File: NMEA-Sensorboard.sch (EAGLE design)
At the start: 15 parts, among them IC1 R-78E05-1.0, IC2 ESP32_D1_MINI, IC3 MCP2562, IC4 INA226, X3 DS1820, X4 DS1820, X5 DS1820, X6 DS1820, X7 BUS

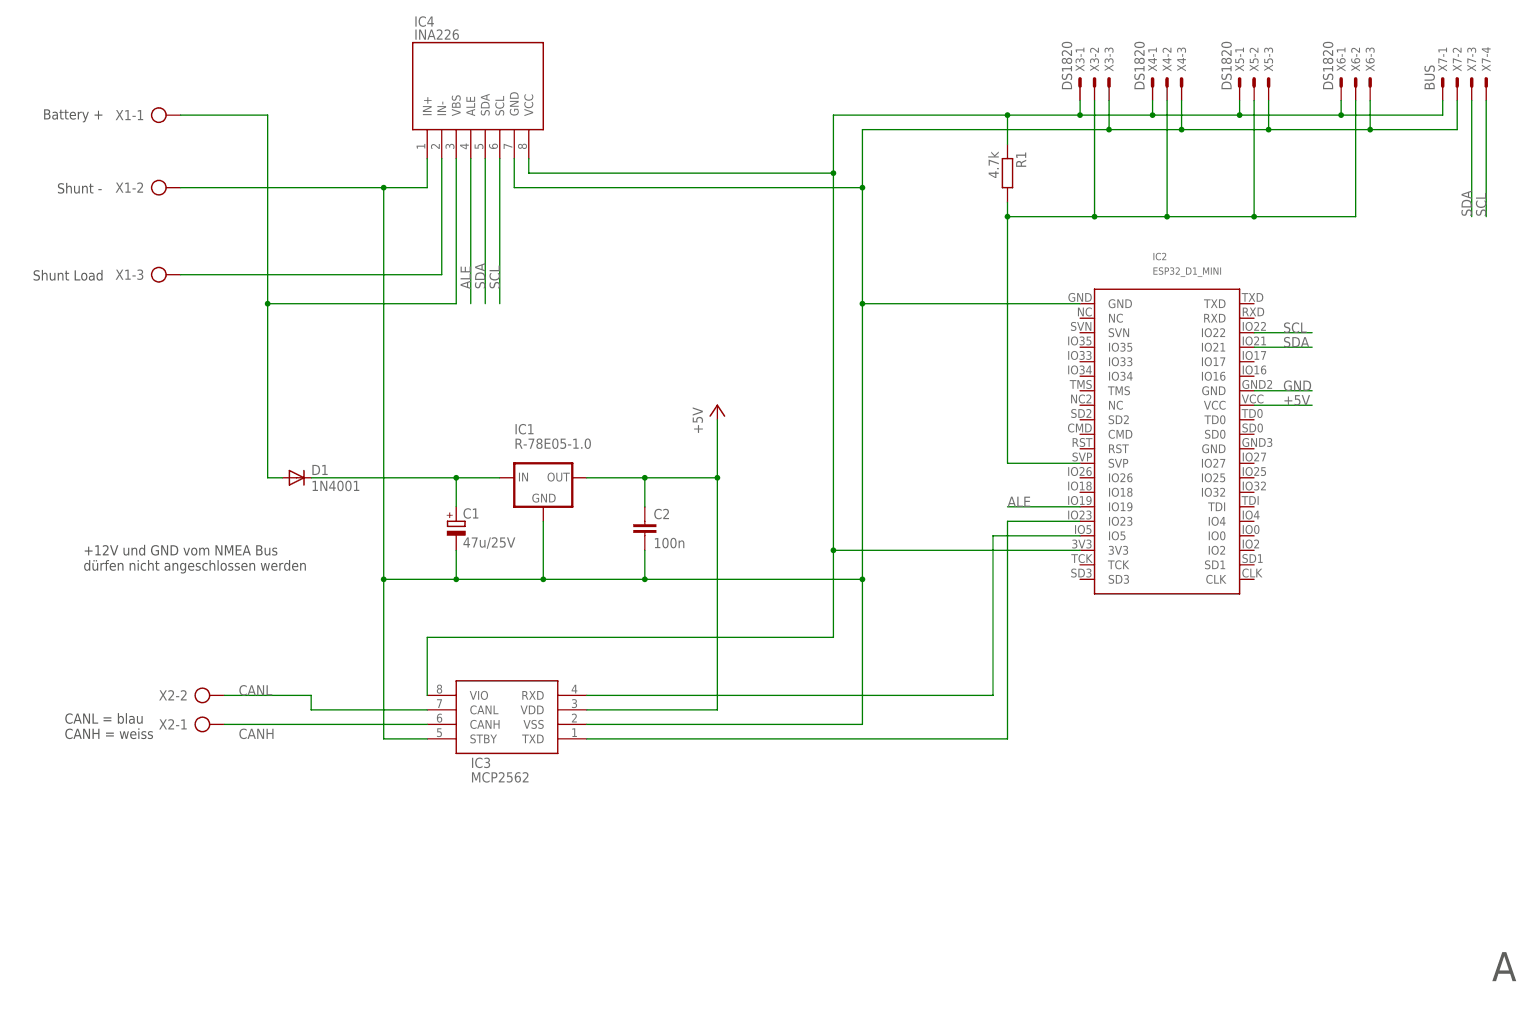
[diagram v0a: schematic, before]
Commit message: refactor: overhaul schematic and PCB layout to fix multiple issues
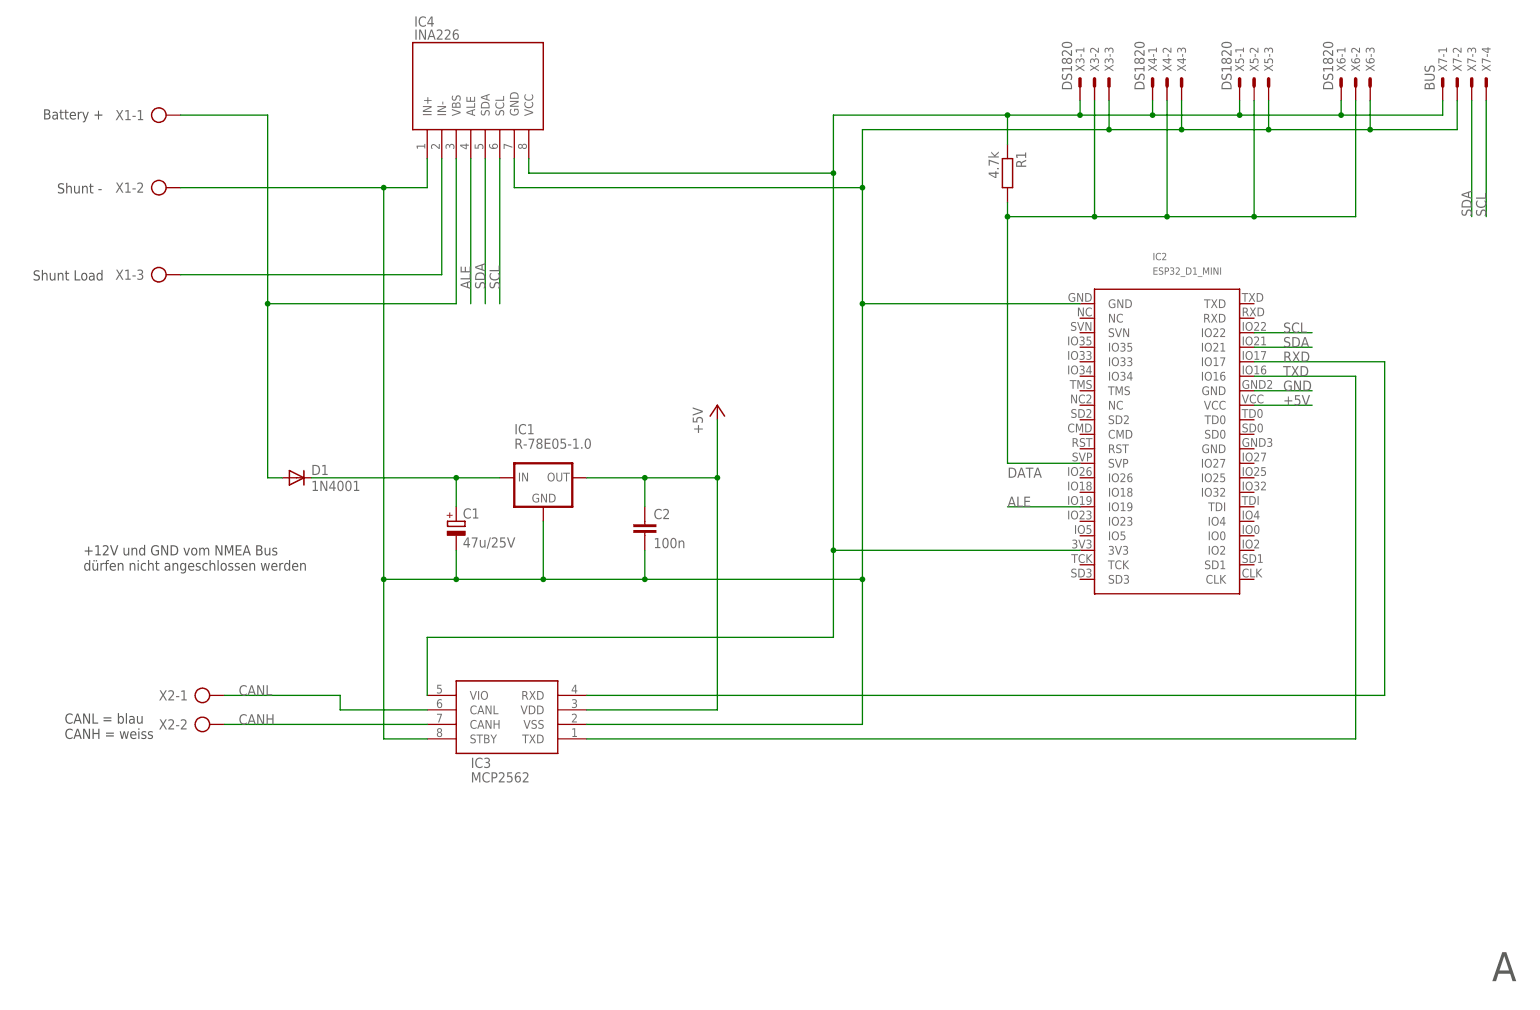
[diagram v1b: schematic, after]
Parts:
- C1: device rcl:CPOL-EUE5-8.5 -> rcl:CPOL-EUE2-5
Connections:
- net N$9 renamed DATA
- net CANH: now also X2-2.KL; no longer X2-1.KL
- net CANL: now also X2-1.KL; no longer X2-2.KL
- net RXD: now also IC2.IO17; no longer IC2.IO5
- net TXD: now also IC2.IO16; no longer IC2.IO23
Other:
- moved on the sheet: X2-1, X2-2
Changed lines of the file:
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@@
 <grid distance="0.1" unitdist="inch" unit="inch" style="lines" multiple="1" display="no" altdistance="0.01" altunitdist="inch" altunit="inch"/>
 <layers>
-<layer number="1" name="Top" color="4" fill="1" visible="no" active="no"/>
-<layer number="16" name="Bottom" color="1" fill="1" visible="no" active="no"/>
-<layer number="17" name="Pads" color="2" fill="1" visible="no" active="no"/>
-<layer number="18" name="Vias" color="2" fill="1" visible="no" active="no"/>
-<layer number="19" name="Unrouted" color="6" fill="1" visible="no" active="no"/>
-<layer number="20" name="Dimension" color="24" fill="1" visible="no" active="no"/>
-<layer number="21" name="tPlace" color="7" fill="1" visible="no" active="no"/>
-<layer number="22" name="bPlace" color="7" fill="1" visible="no" active="no"/>
-<layer number="23" name="tOrigins" color="15" fill="1" visible="no" active="no"/>
-<layer number="24" name="bOrigins" color="15" fill="1" visible="no" active="no"/>
-<layer number="25" name="tNames" color="7" fill="1" visible="no" active="no"/>
-<layer number="26" name="bNames" color="7" fill="1" visible="no" active="no"/>
-<layer number="27" name="tValues" color="7" fill="1" visible="no" active="no"/>
-<layer number="28" name="bValues" color="7" fill="1" visible="no" active="no"/>
+<layer number="1" name="Top" color="4" fill="1" visible="yes" active="no"/>
+<layer number="16" name="Bottom" color="1" fill="1" visible="yes" active="no"/>
+<layer number="17" name="Pads" color="2" fill="1" visible="yes" active="no"/>
+<layer number="18" name="Vias" color="2" fill="1" visible="yes" active="no"/>
+<layer number="19" name="Unrouted" color="6" fill="1" visible="yes" active="no"/>
+<layer number="20" name="Dimension" color="24" fill="1" visible="yes" active="no"/>
+<layer number="21" name="tPlace" color="7" fill="1" visible="yes" active="no"/>
+<layer number="22" name="bPlace" color="7" fill="1" visible="yes" active="no"/>
+<layer number="23" name="tOrigins" color="15" fill="1" visible="yes" active="no"/>
+<layer number="24" name="bOrigins" color="15" fill="1" visible="yes" active="no"/>
+<layer number="25" name="tNames" color="7" fill="1" visible="yes" active="no"/>
+<layer number="26" name="bNames" color="7" fill="1" visible="yes" active="no"/>
+<layer number="27" name="tValues" color="7" fill="1" visible="yes" active="no"/>
+<layer number="28" name="bValues" color="7" fill="1" visible="yes" active="no"/>
 <layer number="29" name="tStop" color="7" fill="3" visible="no" active="no"/>
 <layer number="30" name="bStop" color="7" fill="6" visible="no" active="no"/>
@@
 <layer number="35" name="tGlue" color="7" fill="4" visible="no" active="no"/>
 <layer number="36" name="bGlue" color="7" fill="5" visible="no" active="no"/>
-<layer number="37" name="tTest" color="7" fill="1" visible="no" active="no"/>
-<layer number="38" name="bTest" color="7" fill="1" visible="no" active="no"/>
+<layer number="37" name="tTest" color="7" fill="1" visible="yes" active="no"/>
+<layer number="38" name="bTest" color="7" fill="1" visible="yes" active="no"/>
 <layer number="39" name="tKeepout" color="4" fill="11" visible="no" active="no"/>
 <layer number="40" name="bKeepout" color="1" fill="11" visible="no" active="no"/>
@@
 <layer number="44" name="Drills" color="7" fill="1" visible="no" active="no"/>
 <layer number="45" name="Holes" color="7" fill="1" visible="no" active="no"/>
-<layer number="46" name="Milling" color="3" fill="1" visible="no" active="no"/>
-<layer number="47" name="Measures" color="7" fill="1" visible="no" active="no"/>
-<layer number="48" name="Document" color="7" fill="1" visible="no" active="no"/>
-<layer number="49" name="Reference" color="7" fill="1" visible="no" active="no"/>
-<layer number="51" name="tDocu" color="7" fill="1" visible="no" active="no"/>
-<layer number="52" name="bDocu" color="7" fill="1" visible="no" active="no"/>
+<layer number="46" name="Milling" color="3" fill="1" visible="yes" active="no"/>
+<layer number="47" name="Measures" color="7" fill="1" visible="yes" active="no"/>
+<layer number="48" name="Document" color="7" fill="1" visible="yes" active="no"/>
+<layer number="49" name="Reference" color="7" fill="1" visible="yes" active="no"/>
+<layer number="51" name="tDocu" color="7" fill="1" visible="yes" active="no"/>
+<layer number="52" name="bDocu" color="7" fill="1" visible="yes" active="no"/>
 <layer number="88" name="SimResults" color="9" fill="1" visible="yes" active="yes"/>
 <layer number="89" name="SimProbes" color="9" fill="1" visible="yes" active="yes"/>
@@
 <part name="X6" library="con-molex" library_urn="urn:adsk.eagle:library:165" deviceset="22-23-2031" device="" package3d_urn="urn:adsk.eagle:package:8078634/1" value="DS1820"/>
 <part name="X7" library="con-molex" library_urn="urn:adsk.eagle:library:165" deviceset="22-23-2041" device="" package3d_urn="urn:adsk.eagle:package:8078635/1" value="BUS"/>
-<part name="C1" library="rcl" library_urn="urn:adsk.eagle:library:334" deviceset="CPOL-EU" device="E5-8.5" package3d_urn="urn:adsk.eagle:package:23374/1" value="47u/25V"/>
+<part name="C1" library="rcl" library_urn="urn:adsk.eagle:library:334" deviceset="CPOL-EU" device="E2-5" package3d_urn="urn:adsk.eagle:package:23346/2" value="47u/25V"/>
 <part name="C2" library="rcl" library_urn="urn:adsk.eagle:library:334" deviceset="C-EU" device="050-024X044" package3d_urn="urn:adsk.eagle:package:23643/1" value="100n"/>
 </parts>
@@
 <attribute name="VALUE" x="116.84" y="101.6" size="1.778" layer="96" rot="R90"/>
 </instance>
-<instance part="X2" gate="-1" x="27.94" y="50.8" smashed="yes">
+<instance part="X2" gate="-1" x="27.94" y="55.88" smashed="yes">
+<attribute name="NAME" x="26.67" y="56.769" size="1.778" layer="95" rot="R180"/>
+</instance>
+<instance part="X2" gate="-2" x="27.94" y="50.8" smashed="yes">
 <attribute name="NAME" x="26.67" y="51.689" size="1.778" layer="95" rot="R180"/>
-</instance>
-<instance part="X2" gate="-2" x="27.94" y="55.88" smashed="yes">
-<attribute name="NAME" x="26.67" y="56.769" size="1.778" layer="95" rot="R180"/>
-<attribute name="VALUE" x="24.13" y="52.197" size="1.778" layer="96"/>
+<attribute name="VALUE" x="24.13" y="47.117" size="1.778" layer="96"/>
 </instance>
 <instance part="X4" gate="-1" x="195.58" y="162.56" smashed="yes" rot="R90">
@@
 </busses>
 <nets>
-<net name="RXD" class="0">
-<segment>
-<pinref part="IC3" gate="G$1" pin="RXD"/>
-<wire x1="167.64" y1="55.88" x2="96.52" y2="55.88" width="0.1524" layer="91"/>
-<pinref part="IC2" gate="G$1" pin="IO5"/>
-<wire x1="167.64" y1="83.82" x2="167.64" y2="55.88" width="0.1524" layer="91"/>
-<wire x1="182.88" y1="83.82" x2="167.64" y2="83.82" width="0.1524" layer="91"/>
-</segment>
-</net>
 <net name="GND" class="0">
 <segment>
@@
 </segment>
 </net>
-<net name="N$9" class="0">
+<net name="DATA" class="0">
 <segment>
 <pinref part="R1" gate="G$1" pin="2"/>
@@
 <wire x1="170.18" y1="139.7" x2="170.18" y2="96.52" width="0.1524" layer="91"/>
 <wire x1="170.18" y1="96.52" x2="182.88" y2="96.52" width="0.1524" layer="91"/>
+<label x="170.18" y="93.98" size="1.778" layer="95"/>
 </segment>
 </net>
@@
 <segment>
 <pinref part="IC3" gate="G$1" pin="TXD"/>
-<wire x1="96.52" y1="48.26" x2="170.18" y2="48.26" width="0.1524" layer="91"/>
-<pinref part="IC2" gate="G$1" pin="IO23"/>
-<wire x1="182.88" y1="86.36" x2="170.18" y2="86.36" width="0.1524" layer="91"/>
-<wire x1="170.18" y1="48.26" x2="170.18" y2="86.36" width="0.1524" layer="91"/>
+<wire x1="96.52" y1="48.26" x2="231.14" y2="48.26" width="0.1524" layer="91"/>
+<pinref part="IC2" gate="G$1" pin="IO16"/>
+<wire x1="231.14" y1="48.26" x2="231.14" y2="111.76" width="0.1524" layer="91"/>
+<wire x1="231.14" y1="111.76" x2="213.36" y2="111.76" width="0.1524" layer="91"/>
+<label x="218.44" y="111.76" size="1.778" layer="95"/>
+</segment>
+</net>
+<net name="RXD" class="0">
+<segment>
+<pinref part="IC3" gate="G$1" pin="RXD"/>
+<wire x1="96.52" y1="55.88" x2="236.22" y2="55.88" width="0.1524" layer="91"/>
+<pinref part="IC2" gate="G$1" pin="IO17"/>
+<wire x1="236.22" y1="55.88" x2="236.22" y2="114.3" width="0.1524" layer="91"/>
+<wire x1="236.22" y1="114.3" x2="213.36" y2="114.3" width="0.1524" layer="91"/>
+<label x="218.44" y="114.3" size="1.778" layer="95"/>
 </segment>
 </net>
 <net name="CANL" class="0">
 <segment>
+<pinref part="IC3" gate="G$1" pin="CANL"/>
+<wire x1="68.58" y1="53.34" x2="53.34" y2="53.34" width="0.1524" layer="91"/>
+<pinref part="X2" gate="-1" pin="KL"/>
+<wire x1="53.34" y1="53.34" x2="53.34" y2="55.88" width="0.1524" layer="91"/>
+<wire x1="53.34" y1="55.88" x2="33.02" y2="55.88" width="0.1524" layer="91"/>
+<label x="35.56" y="55.88" size="1.778" layer="95"/>
+</segment>
+</net>
+<net name="CANH" class="0">
+<segment>
+<pinref part="IC3" gate="G$1" pin="CANH"/>
 <pinref part="X2" gate="-2" pin="KL"/>
-<wire x1="33.02" y1="55.88" x2="48.26" y2="55.88" width="0.1524" layer="91"/>
-<wire x1="48.26" y1="55.88" x2="48.26" y2="53.34" width="0.1524" layer="91"/>
-<pinref part="IC3" gate="G$1" pin="CANL"/>
-<wire x1="48.26" y1="53.34" x2="68.58" y2="53.34" width="0.1524" layer="91"/>
-<label x="35.56" y="55.88" size="1.778" layer="95"/>
-</segment>
-</net>
-<net name="CANH" class="0">
-<segment>
-<pinref part="X2" gate="-1" pin="KL"/>
-<pinref part="IC3" gate="G$1" pin="CANH"/>
-<wire x1="33.02" y1="50.8" x2="68.58" y2="50.8" width="0.1524" layer="91"/>
-<label x="35.56" y="48.26" size="1.778" layer="95"/>
-</segment>
-</net>
+<wire x1="68.58" y1="50.8" x2="33.02" y2="50.8" width="0.1524" layer="91"/>
+<label x="35.56" y="50.8" size="1.778" layer="95"/>
+</segment>
+</net>
